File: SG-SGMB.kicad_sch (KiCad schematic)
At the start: 1 part, among them U1 ESP32-S3

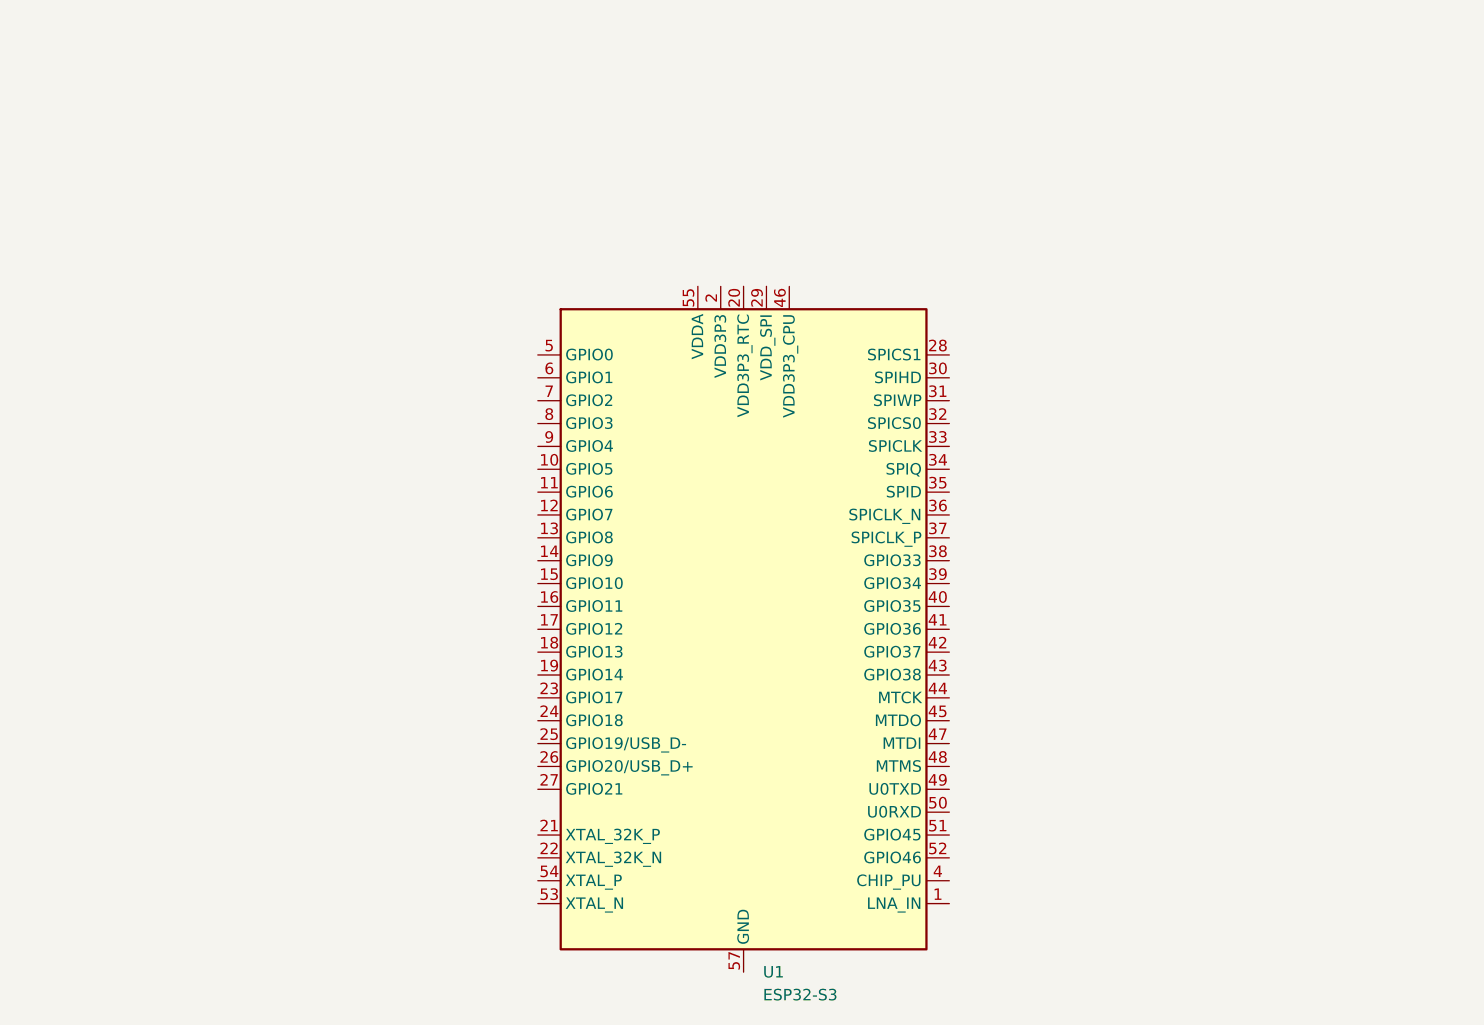
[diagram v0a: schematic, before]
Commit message: feat: Add stack header for connection between board and RPi.
Currently has the datasheet for the header to be used. Require to find SMD ceremic and catalytic capacitors for safe boot for the RPi.
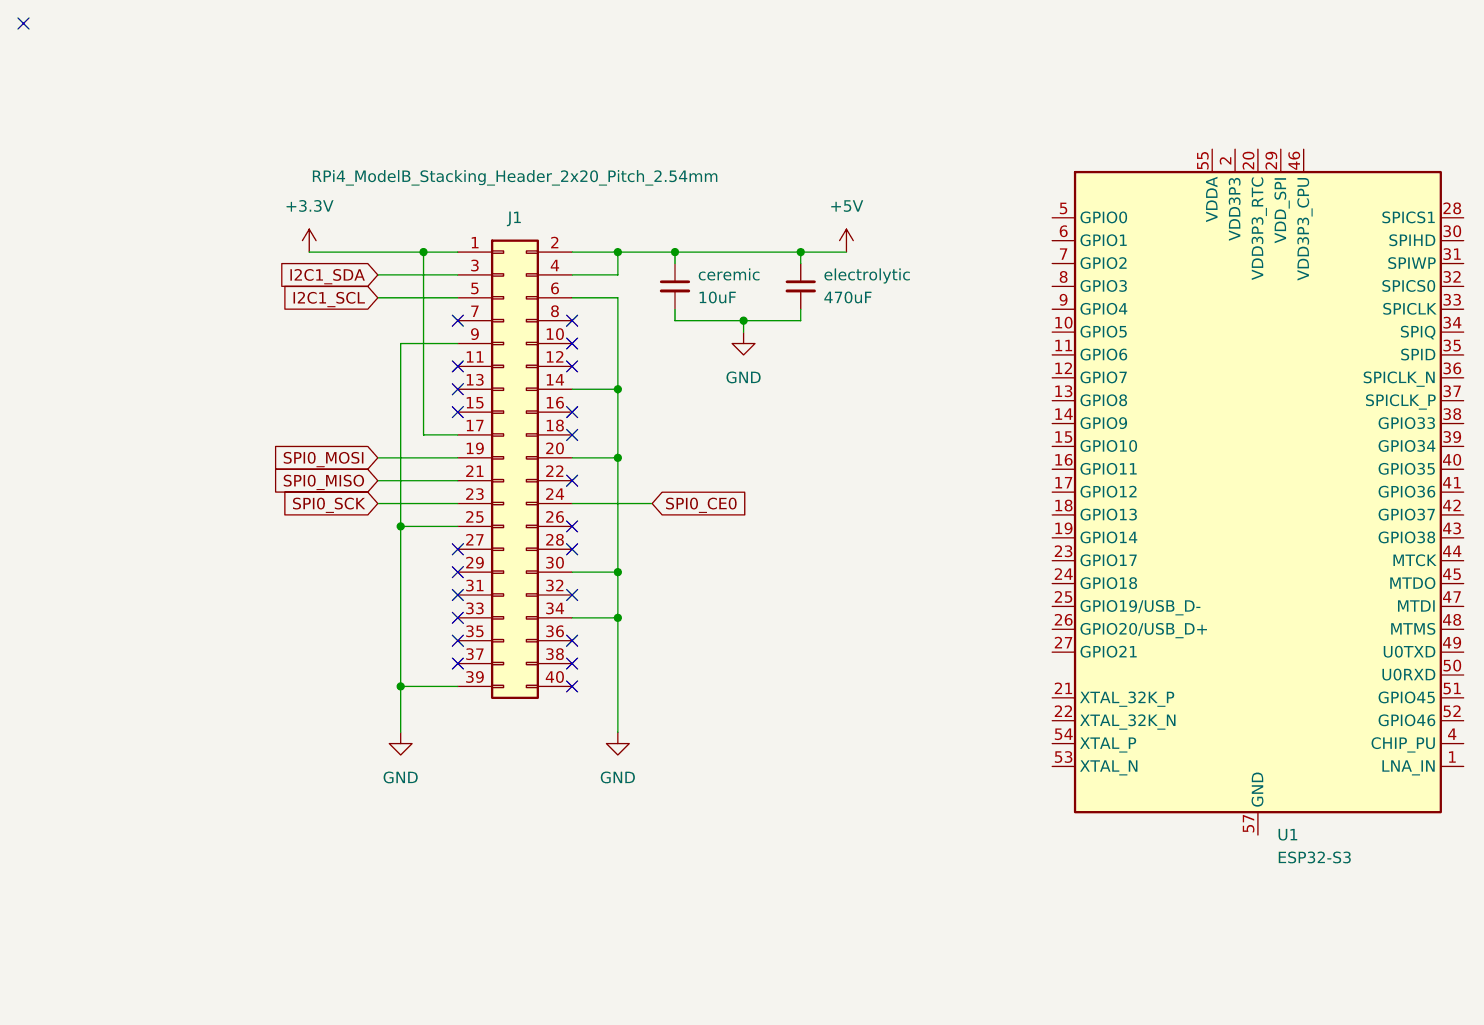
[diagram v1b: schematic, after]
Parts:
- added RPi4_ModelB_Stacking_Header_2x20_Pitch_2.54mm: J1, Connector_PinHeader_2.54mm:PinHeader_2x20_P2.54mm_Vertical, symbol Connector_Generic:Conn_02x20_Row_Letter_Last
- added ceremic: 10uF, symbol Device:C_Small
- added electrolytic: 470uF, symbol Device:C_Small
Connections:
- new net +3.3V: RPi4_ModelB_Stacking_Header_2x20_Pitch_2.54mm.1 (3v3), RPi4_ModelB_Stacking_Header_2x20_Pitch_2.54mm.17 (3v3)
- new net +5V: RPi4_ModelB_Stacking_Header_2x20_Pitch_2.54mm.2 (5V), RPi4_ModelB_Stacking_Header_2x20_Pitch_2.54mm.4 (5V), ceremic.1, electrolytic.1
- new net GND: RPi4_ModelB_Stacking_Header_2x20_Pitch_2.54mm.14 (GND), RPi4_ModelB_Stacking_Header_2x20_Pitch_2.54mm.20 (GND), RPi4_ModelB_Stacking_Header_2x20_Pitch_2.54mm.25 (GND), RPi4_ModelB_Stacking_Header_2x20_Pitch_2.54mm.30 (GND), RPi4_ModelB_Stacking_Header_2x20_Pitch_2.54mm.34 (GND), RPi4_ModelB_Stacking_Header_2x20_Pitch_2.54mm.39 (GND), RPi4_ModelB_Stacking_Header_2x20_Pitch_2.54mm.6 (GND), RPi4_ModelB_Stacking_Header_2x20_Pitch_2.54mm.9 (GND), ceremic.2, electrolytic.2
- new net I2C1_SCL: RPi4_ModelB_Stacking_Header_2x20_Pitch_2.54mm.5 (GPIO3)
- new net I2C1_SDA: RPi4_ModelB_Stacking_Header_2x20_Pitch_2.54mm.3 (GPIO2)
- new net SPI0_CE0: RPi4_ModelB_Stacking_Header_2x20_Pitch_2.54mm.24 (GPIO8)
- new net SPI0_MISO: RPi4_ModelB_Stacking_Header_2x20_Pitch_2.54mm.21 (GPIO9)
- new net SPI0_MOSI: RPi4_ModelB_Stacking_Header_2x20_Pitch_2.54mm.19 (GPIO10)
- new net SPI0_SCK: RPi4_ModelB_Stacking_Header_2x20_Pitch_2.54mm.23 (GPIO11)
- no-connect marks 0 -> 23
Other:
- moved on the sheet: U1
